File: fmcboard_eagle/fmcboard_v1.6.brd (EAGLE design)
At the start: 147 x 74 mm, 281 parts, among them IC1 OPA699ID, IC10 LM358, IC11 7805DT, IC12 SN74AUC2G66DCTR, IC13 SN74AUC2G66DCTR, IC14 SN74AUC2G66DCTR, IC15 SN74AUC2G66DCTR, IC16 DAC7578SPWR, IC17 SN74AUC2G66DCTR, IC18 SN74AUC2G66DCTR, IC19 SN74AUC2G66DCTR, IC2 DAC7578SPWR, IC20 SN74AUC2G66DCTR, IC21 74AUP2GU04GW, IC22 74AUP2GU04GW, IC23 74AUP2GU04GW, IC24 74AUP2GU04GW, IC25 MC7905ACD2TR4G, IC26 AMS1117-1.8, IC27 LM358, IC28 SN74AUC2G66DCTR, IC29 LM337KVURG3, IC3 LTC6229IMS8E#TRPBF, IC30 SN74AUC2G66DCTR, IC31 SN74AUC2G66DCTR, IC32 SN74AUC2G66DCTR, IC33 LTC6229IMS8E#TRPBF, IC34 74AUP2GU04GW, IC35 74AUP2GU04GW, IC4 OPA695IDR, IC5 LTC6229IMS8E#TRPBF, IC6 OPA695IDR, IC7 OPA699ID, IC8 LM358, IC9 LM358, J1 8pin, J12 4p-2.54, J13 4p-2.54, J2 ASP-134604-01, J3 4p-2.54, J4 4p-2.54, J5 4p-2.54, J6 4p-2.54, J7 4p-2.54, J8 4p-2.54

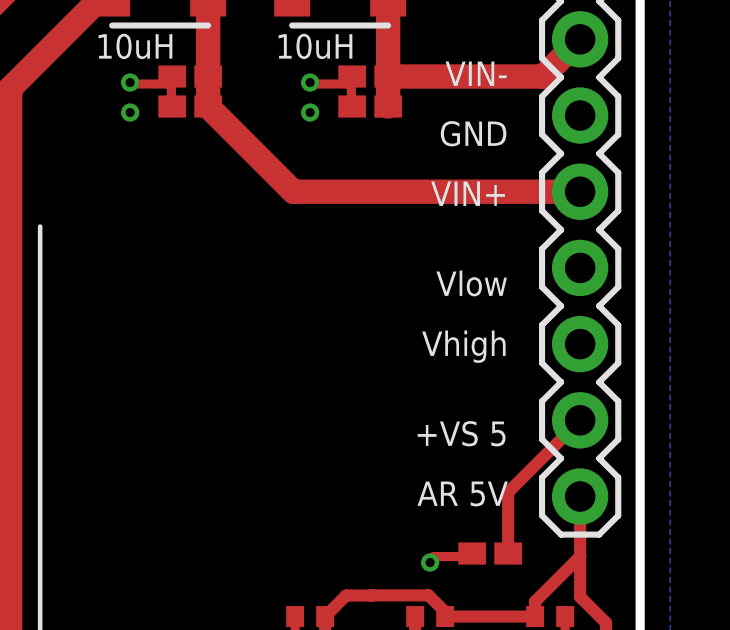
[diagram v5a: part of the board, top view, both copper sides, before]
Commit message: cosmetic updates to v1.65
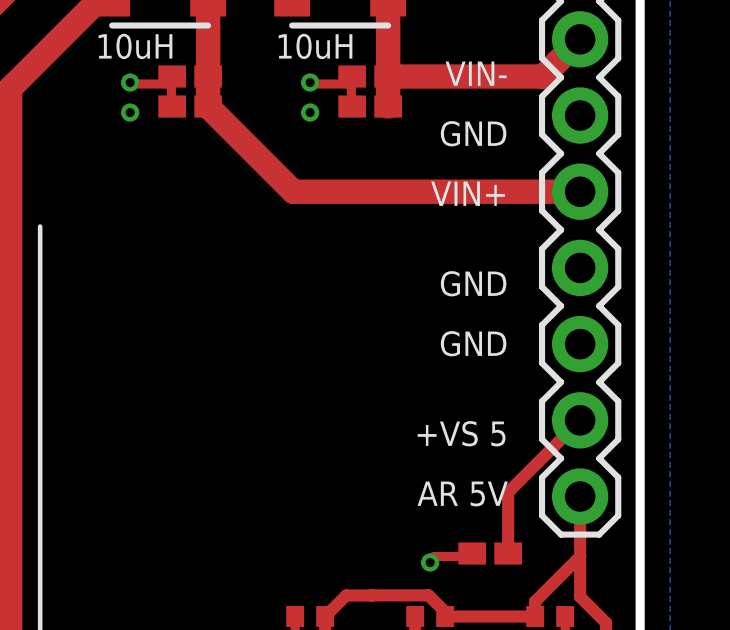
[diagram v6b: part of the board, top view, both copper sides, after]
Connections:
- net DACOFFSET renamed DACOFFSETP
- net DACOFFSETOUT_N renamed DACOFFSETNI
- net DACOFFSET_N renamed DACOFFSETN
- net PULSEOFFSET_N renamed PULSEOFFSETN
- net PULSEOFFSET_NI renamed PULSEOFFSETNI
- net PULSEOFFSET_P renamed PULSEOFFSETP
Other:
- board text removed: "Vhigh"
- board text removed: "Vlow"
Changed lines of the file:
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@@
 <text x="36.6" y="70.5" size="0.8128" layer="21" rot="R180">12V</text>
 <text x="21.6" y="70.5" size="0.8128" layer="21" rot="R180">GND</text>
-<text x="142.6" y="59.5" size="0.8128" layer="21" rot="R180">Vhigh</text>
+<text x="142.6" y="59.5" size="0.8128" layer="21" rot="R180">GND</text>
 <text x="69.5" y="57.4" size="0.8128" layer="21" rot="R90">GND</text>
 <text x="142.6" y="71.5" size="0.8128" layer="21" rot="R180">GND</text>
@@
 <text x="142.6" y="66.5" size="0.8128" layer="21" rot="R180">GND</text>
 <text x="142.6" y="64.5" size="0.8128" layer="21" rot="R180">VIN+</text>
-<text x="142.6" y="61.5" size="0.8128" layer="21" rot="R180">Vlow</text>
+<text x="142.6" y="61.5" size="0.8128" layer="21" rot="R180">GND</text>
 <text x="142.6" y="56.5" size="0.8128" layer="21" rot="R180">+VS 5</text>
 <text x="142.6" y="54.5" size="0.8128" layer="21" rot="R180">AR 5V</text>
@@
 <wire x1="94.711" y1="56.365" x2="100.289" y2="56.365" width="0.3048" layer="1"/>
 </signal>
-<signal name="DACOFFSET">
+<signal name="DACOFFSETP">
 <contactref element="R31" pad="2"/>
 <contactref element="IC16" pad="4"/>
@@
 <wire x1="44.875" y1="34.125" x2="44.875" y2="34" width="0.3048" layer="1"/>
 </signal>
-<signal name="PULSEOFFSET_P">
+<signal name="PULSEOFFSETP">
 <contactref element="R79" pad="2"/>
 <contactref element="IC16" pad="13"/>
@@
 <via x="52.625" y="44.75" extent="1-16" drill="0.3048"/>
 </signal>
-<signal name="PULSEOFFSET_N">
+<signal name="PULSEOFFSETN">
 <contactref element="R61" pad="2"/>
 <contactref element="IC16" pad="5"/>
@@
 <via x="46.75" y="41.875" extent="1-16" drill="0.3048"/>
 </signal>
-<signal name="PULSEOFFSET_NI">
+<signal name="PULSEOFFSETNI">
 <contactref element="R85" pad="2"/>
 <contactref element="R35" pad="2"/>
@@
 <via x="90" y="13.75" extent="1-16" drill="0.3048"/>
 </signal>
-<signal name="DACOFFSET_N">
+<signal name="DACOFFSETN">
 <contactref element="IC16" pad="12"/>
 <contactref element="R17" pad="2"/>
@@
 <via x="57.5" y="36.125" extent="1-16" drill="0.3048"/>
 </signal>
-<signal name="DACOFFSETOUT_N">
+<signal name="DACOFFSETNI">
 <contactref element="R115" pad="2"/>
 <contactref element="IC10" pad="7"/>

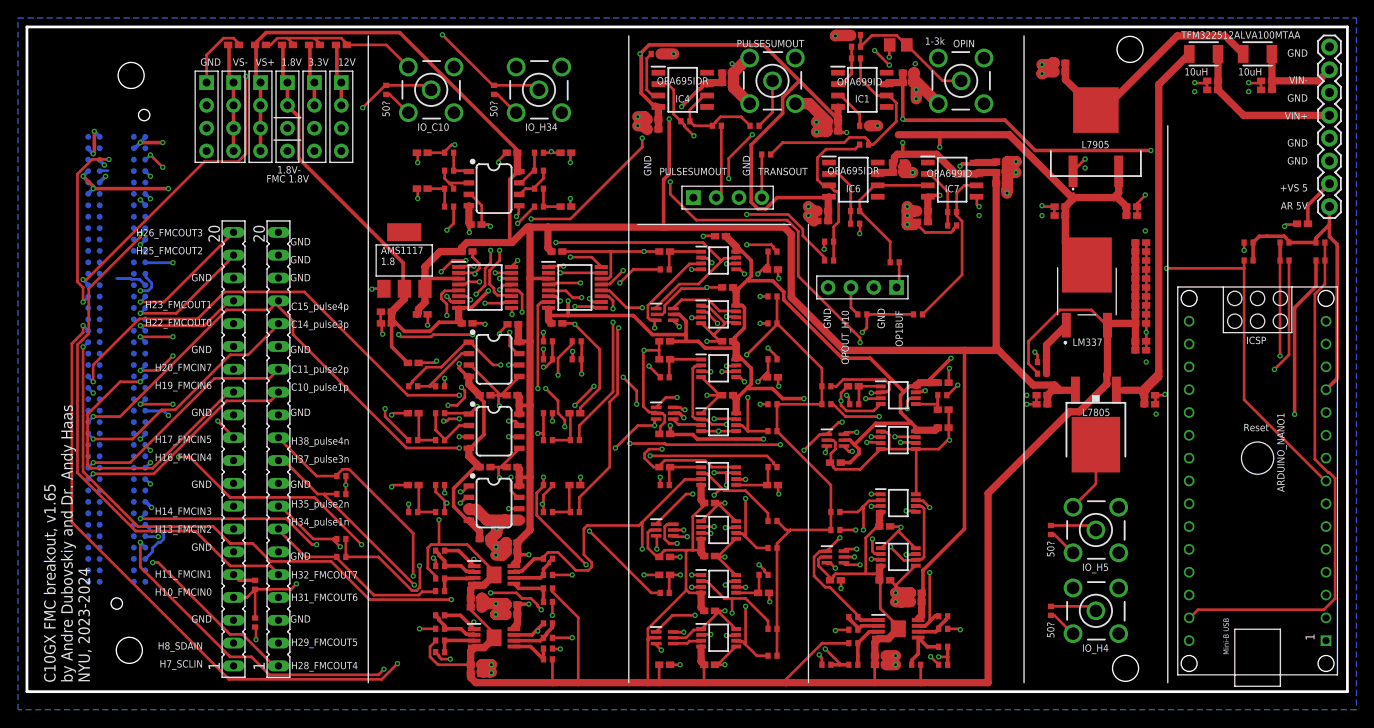
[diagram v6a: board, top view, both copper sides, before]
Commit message: move 1.65s to 1.6
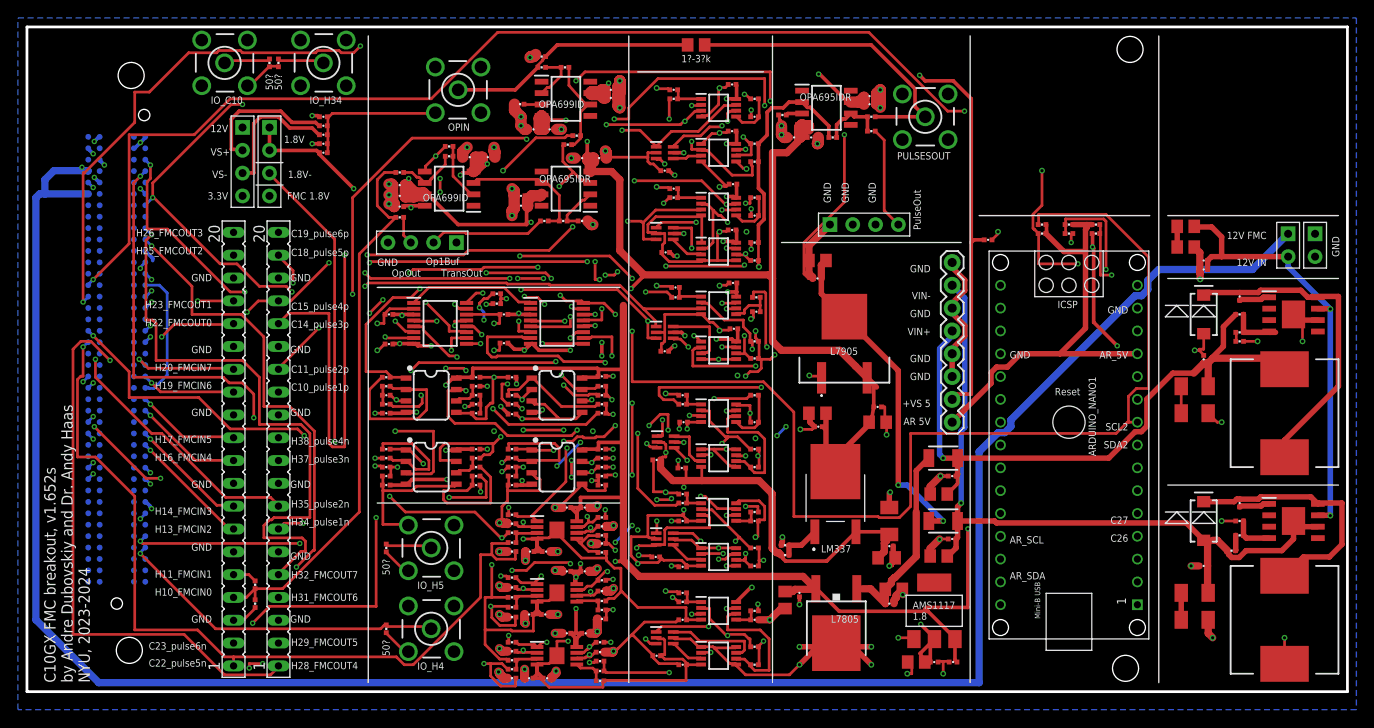
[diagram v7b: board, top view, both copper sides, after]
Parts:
- removed C112, C113, C114, C115, C2, C40: 10uF, rcl:C0402K
- removed J4, J6, J7: 4p-2.54, Seeed-Connector:H4-2.54
- removed PULSESUMOUT: BU-SMB-V, con-coax:BU-SMB-V
- added C11, C121, C8: 0.1uF, passives:0402_CAP
- added C120, C64: 10uF, rcl:C0805
- added C122: 0.01uF, passives:0402_CAP
- added C123, C124, C125: 100uF, rcl:C1206K
- added D1, D2: B340A, SparkFun-DiscreteSemi:SMA-DIODE
- added IC36, IC37: TPS5430DDAR, TPS5430DDAR:SOIC127P600X170-9N
- added J9: 2p-2.54, Seeed-Connector:H2-2.54
- added L3, L4: 10uH, SparkFun-Passives:CDRH125
- added PULSESOUT: BU-SMB-V, con-coax:BU-SMB-V
- added R116, R117, R60, R84: 1k, passives:0402_RES
- added R118, R73: 10k, passives:0402_RES
- C1, C110, C111, C34, C38, C39, C41, C77, C86: device rcl:C0402K -> rcl:C0805
- C10, C100, C101, C102, C103, C104, C105, C116, C117, C12, C13, C14, C15, C16, C17, C18, C19, C20, C21, C22, C23, C24, C25, C26, C27, C28, C29, C3, C30, C31, C32, C33, C35, C36, C37, C4, C42, C43, C44, C45, C46, C47, C48, C49, C5, C50, C51, C52, C53, C54, C55, C56, C57, C58, C59, C6, C60, C61, C62, C63, C65, C66, C67, C68, C69, C7, C70, C71, C72, C73, C74, C75, C76, C78, C79, C81, C82, C83, C84, C85, C87, C88, C89, C9, C90, C91, C92, C93, C94, C95, C96, C97, C98, C99: device rcl:C0402K -> passives:0402_CAP
- C106: value 10uF -> 0.1uF; device rcl:C0402K -> passives:0402_CAP
- C107: value 10uF -> 0.01uF; device rcl:C0402K -> passives:0402_CAP
- C108, C109: value 10uF -> 100uF; device rcl:C0402K -> rcl:C1206K
- J3: value 4p-2.54 -> 2p-2.54; device Seeed-Connector:H4-2.54 -> Seeed-Connector:H2-2.54
- R1, R10, R100, R101, R102, R103, R104, R105, R106, R107, R108, R109, R11, R110, R111, R112, R113, R114, R115, R12, R13, R14, R15, R16, R17, R18, R19, R2, R20, R21, R22, R23, R24, R25, R26, R27, R28, R29, R3, R30, R31, R32, R33, R34, R35, R36, R37, R38, R39, R4, R40, R41, R42, R43, R44, R45, R46, R47, R48, R49, R5, R50, R51, R52, R53, R54, R55, R56, R57, R58, R59, R6, R61, R62, R63, R64, R65, R66, R67, R68, R69, R7, R70, R71, R72, R74, R75, R76, R77, R78, R79, R8, R80, R81, R82, R83, R85, R86, R87, R88, R89, R90, R91, R92, R93, R94, R95, R96, R97, R98, R99: device rcl:R0402 -> passives:0402_RES
- R9: value 1-3k -> 1?-3?k; device resistor:R0805 -> rcl:R0805
- moved J3 112.3 mm to (143.4, 49.7)
- moved IO_H4 74.0 mm to (45.0, 7.00)
- moved IO_H5 74.0 mm to (45.0, 16.0)
- moved R15 74.0 mm to (40.0, 7.00)
- moved R16 74.0 mm to (40.0, 16.0)
- moved C74 71.7 mm to (101.0, 3.30), turned to 0 degrees
- moved C34 70.7 mm to (99.0, 3.30)
- moved IC26 70.7 mm to (101.0, 9.00)
- moved C3 70.6 mm to (103.1, 3.30), turned to 180 degrees
- moved C7 67.2 mm to (41.5, 54.0), turned to 180 degrees
- moved C87 67.1 mm to (41.5, 55.2), turned to 180 degrees
- moved C28 67.0 mm to (41.5, 56.4), turned to 180 degrees
- moved C41 63.4 mm to (101.5, 15.1)
- moved L2 62.7 mm to (102.0, 19.0)
- moved C44 61.9 mm to (103.0, 17.0)
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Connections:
- removed net N$35: J13.2, R71.1
- removed net N$38: J13.4, R72.1
- new net ARVIN: ARDUINO_NANO1.15
- new net BOOT1: C122.1, IC37.1
- new net BOOT2: C107.1, IC36.1
- new net FB1: IC37.4, R60.2, R73.1
- new net FB2: IC36.4, R116.2, R118.1
- new net N$29: C120.1, C64.2
- new net N$36: J5.2, R72.1
- new net N$53: C123.1, C124.2
- new net N$54: R60.1, R84.2
- new net N$55: C108.1, C109.2
- new net N$56: R116.1, R117.2
- new net N$57: J13.4, R71.1
- new net SW1: C122.2, D1.C, IC37.8, L3.1
- new net SW2: C107.2, D2.C, IC36.8, L4.1
- net 12V: now also J9.1; no longer J8.2, J8.3, J8.4
- net 1V8-: now also C125.1; no longer C106.1, C107.1, C108.1, C109.1, C110.1, C111.1, C112.1, C113.1, C114.1, C115.1
- net 3V3: now also J8.4; no longer J3.1, J3.2, J3.3, J3.4
- net C18: now also SV2.19
- net C19: now also SV2.20
- net C22: now also SV1.1
- net C23: now also SV1.2
- net GND: now also C106.1, C109.1, C11.2, C111.1, C120.2, C121.2, C123.2, C125.2, C8.2, D1.A, IC37.6, IC37.9, J13.2, J3.1, J3.2, L4.2, PULSESOUT.2, PULSESOUT.3, PULSESOUT.4, PULSESOUT.5, R118.2, R84.1; no longer C106.2, C107.2, C108.2, C109.2, C111.2, C112.2, C113.2, C114.2, C115.2, C2.2, C40.1, J4.1, J4.2, J4.3, J4.4, J5.2, PULSESUMOUT.2, PULSESUMOUT.3, PULSESUMOUT.4, PULSESUMOUT.5, SV2.19, SV2.20
- net OP1BUF: now also R72.2; no longer R89.2
- net PULSEOUT: now also PULSESOUT.1; no longer PULSESUMOUT.1
- net SCLIN: no longer SV1.1
- net SDAIN: no longer SV1.2
- net TRANSOUT: now also R89.2; no longer R72.2
- net VIN: now also C11.1, C64.1, C8.1, IC36.7, IC37.7, J9.2; no longer ARDUINO_NANO1.15
- net VIN+: now also C121.1, C124.1, L3.2, R73.2
- net VIN+CLEAN: now also C110.1; no longer C2.1
- net VIN-: now also C106.2, C108.2, D2.A, IC36.6, IC36.9, R117.1
- net VIN-CLEAN: now also C111.2; no longer C40.2
- net VS+: now also J8.2; no longer J6.1, J6.2, J6.3, J6.4
- net VS-: now also J8.3; no longer J7.1, J7.2, J7.3, J7.4
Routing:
- net 12V: track 45.1 -> 269.7 mm, vias 3 -> 2
- net GND: track 448.3 -> 625.9 mm, vias 114 -> 129
- net N$46: track 3.75 -> 116.4 mm, vias 0 -> 4
- net H5: track 133.7 -> 38.7 mm, vias 1 -> 2
- net H4: track 124.5 -> 37.1 mm, vias 2 -> 1
- net 1V8-: track 353.9 -> 271.8 mm, vias 1 -> 11
- net DACN5I: track 84.9 -> 2.76 mm, vias 4 -> 0
- net VIN-: track 10.9 -> 83.8 mm, vias 0 -> 1
- net DACN6I: track 75.7 -> 6.30 mm, vias 2 -> 0
- net VIN+: track 21.6 -> 81.0 mm, vias 0 -> 1
- net VIN: track 0.00 -> 49.6 mm, vias 0 -> 2
- net N$21: track 21.8 -> 66.9 mm
- net DACOFFSETNI: track 64.1 -> 21.8 mm, vias 5 -> 4
- net C14: track 85.7 -> 127.8 mm, vias 5 -> 7
- net N$45: track 4.28 -> 44.9 mm, vias 0 -> 4
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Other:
- board text added: "12V FMC"
- board text added: "12V IN"
- board text added: "AR_5V"
- board text added: "AR_SCL"
- board text added: "AR_SDA"
- board text added: "C10GX FMC breakout, v1.652s by Andre Dubovskiy and Dr. Andy Haas NYU, 2023-2024"
- board text added: "C18_pulse5p"
- board text added: "C19_pulse6p"
- board text added: "C22_pulse5n"
- board text added: "C23_pulse6n"
- board text added: "C26"
- board text added: "C27"
- board text added: "Op1Buf"
- board text added: "OpOut"
- board text added: "PulseOut"
- board text added: "SCL2"
- board text added: "SDA2"
- board text added: "TransOut"
- board text removed: "C10GX FMC breakout, v1.65 by Andre Dubovskiy and Dr. Andy Haas NYU, 2023-2024"
- board text removed: "H7_SCLIN"
- board text removed: "H8_SDAIN"
- board text removed: "OP1BUF"
- board text removed: "OPOUT_H10"
- board text removed: "PULSESUMOUT"
- board text removed: "TRANSOUT"

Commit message: tantalum 100uF
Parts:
- removed C108, C109, C123, C124: 100uF, rcl:C1206K
- added C2, C40: 100uF, SparkFun-Passives:VISHAY_C
- moved C110 1.53 mm to (95.7, 12.7)
- moved C43 1.32 mm to (94.7, 10.0)
- moved R117 0.40 mm to (134.1, 16.1)
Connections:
- removed net N$53: C123.1, C124.2
- removed net N$55: C108.1, C109.2
- net GND: now also C2.-, C40.+; no longer C109.1, C123.2
- net VIN+: now also C2.+; no longer C124.1
- net VIN-: now also C40.-; no longer C108.2
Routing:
- net GND: track 625.9 -> 570.0 mm, vias 129 -> 127
- net VIN-: track 83.8 -> 92.5 mm
- net 1V8: track 215.7 -> 212.3 mm
- net VIN+CLEAN: track 27.4 -> 30.7 mm
- net N$55: track 3.00 -> 0.00 mm
- net N$53: track 3.00 -> 0.00 mm
- net VIN+: track 81.0 -> 83.4 mm
- net SW2: track 28.4 -> 27.9 mm
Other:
- board text added: "C10GX FMC breakout, v1.66 by Andre Dubovskiy and Dr. Andy Haas NYU, 2023-2024"
- board text removed: "C10GX FMC breakout, v1.652s by Andre Dubovskiy and Dr. Andy Haas NYU, 2023-2024"
